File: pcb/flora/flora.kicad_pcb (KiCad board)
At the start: 4 copper layers, 59 x 59 mm, 81 parts, among them IC1 ESP32-WROOM-32E(8MB), IC2 SHT20, IC3 TP4056X, IC4 FS8205A, IC5 DW01+G, IC6 TPS63051RMWR, IC7 XC6227C331MR-G, J1 KF350-3.5-2P, J2 KF350-3.5-2P, J3 KF350-3.5-2P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

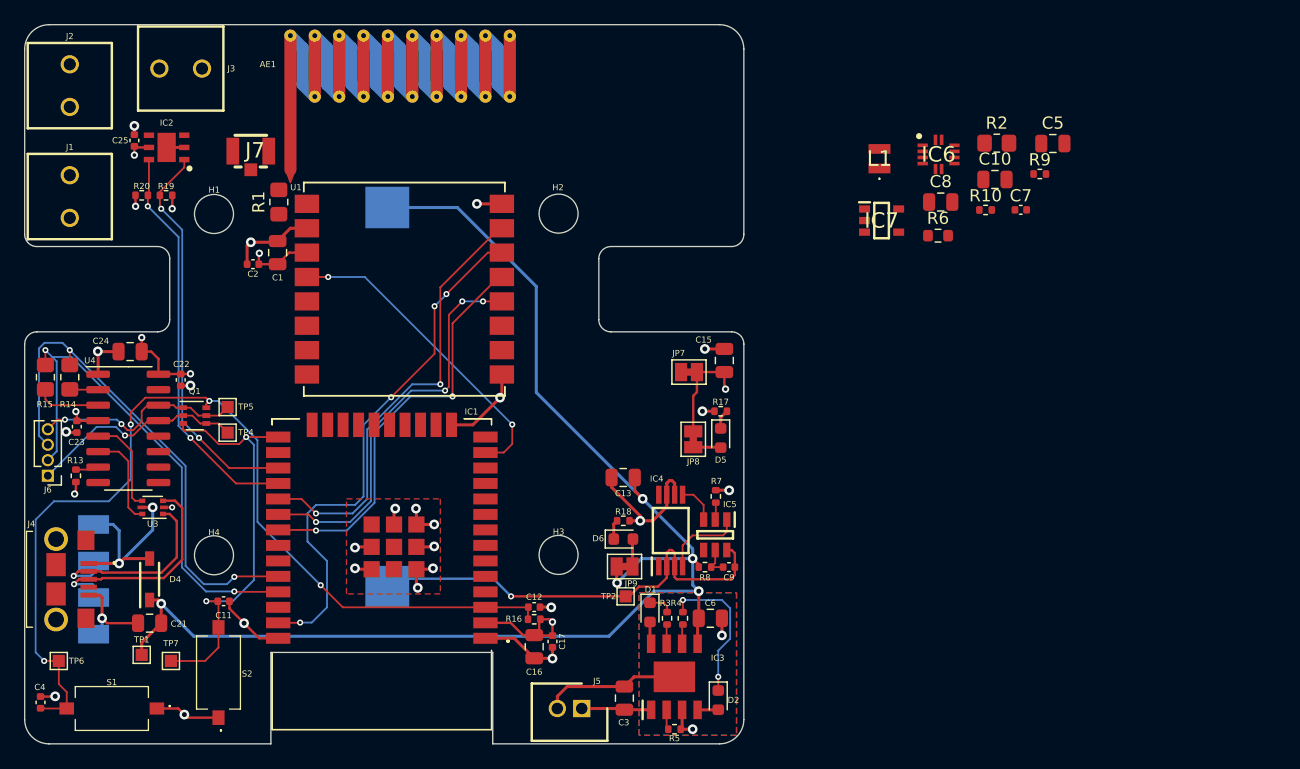
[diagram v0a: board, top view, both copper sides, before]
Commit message: replaced ra 01 with rfm95
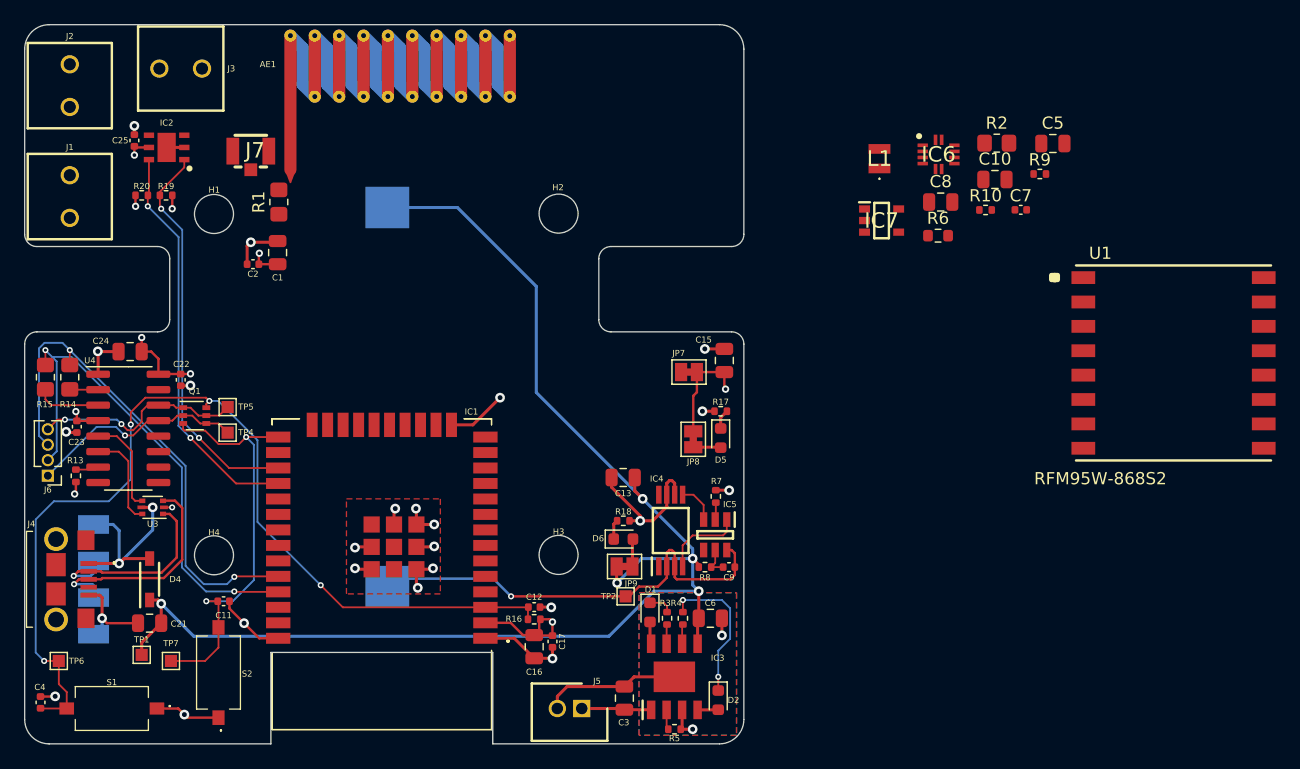
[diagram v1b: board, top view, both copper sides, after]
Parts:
- U1: value Ai-Thinker-Ra-01H -> RFM95W-868S2; footprint RF_Module:Ai-Thinker-Ra-01-LoRa -> personal:RFM95W
- moved U1 63.4 mm to (268.7, 134.1)
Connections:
- J7 pad 3: Net-(U1-Pad1) -> Net-(J7-Pad3)
- R1 pad 1: Net-(U1-Pad1) -> Net-(J7-Pad3)
- U1 pad 1: Net-(U1-Pad1) -> GND
- U1 pad 10: unconnected-(U1-Pad10) -> GND
- U1 pad 12: GPIO18 -> unconnected-(U1-Pad12)
- U1 pad 13: GPIO19 -> +3V3
- U1 pad 14: GPIO23 -> GPIO2
- U1 pad 15: GPIO5 -> unconnected-(U1-Pad15)
- U1 pad 16: GND -> unconnected-(U1-Pad16)
- U1 pad 2: GND -> GPIO19
- U1 pad 3: +3V3 -> GPIO23
- U1 pad 4: GPIO14 -> GPIO18
- U1 pad 5: GPIO2 -> GPIO5
- U1 pad 6: unconnected-(U1-Pad6) -> GPIO14
- U1 pad 8: unconnected-(U1-Pad8) -> GND
- U1 pad 9: GND -> Net-(J7-Pad3)
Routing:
- net GPIO23: track 43.4 -> 0.00 mm, vias 4 -> 0
- net GPIO5: track 35.6 -> 0.00 mm, vias 2 -> 0
- net GPIO19: track 33.6 -> 0.00 mm, vias 2 -> 0
- net GPIO18: track 32.9 -> 0.00 mm, vias 4 -> 0
- net GPIO14: track 26.0 -> 0.00 mm, vias 2 -> 0
- net GND: track 88.0 -> 81.1 mm, vias 28 -> 27
- net +3V3: track 37.5 -> 34.7 mm
- net VDD: track 115.7 -> 113.7 mm
